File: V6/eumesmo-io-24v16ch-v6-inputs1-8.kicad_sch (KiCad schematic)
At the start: 10 parts, among them U12 OR-3H7-4

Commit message: Renamed all files to eumesmo branding
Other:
- title: ESP 24V 16xIn/16xOut/1-Wire Module -> eumesmo 24V 16xIn/16xOut/1-Wire Module
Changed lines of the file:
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@@
 	(paper "A4")
 	(title_block
-		(title "ESP 24V 16xIn/16xOut/1-Wire Module")
-		(date "2026-02-10")
-		(rev "V6.1")
+		(title "eumesmo 24V 16xIn/16xOut/1-Wire Module")
+		(date "2026-06-13")
+		(rev "V6.2")
 	)
 	(text "I_{LED} = (24V - V_{LED}) / 10k\nI_{LED} = (24V - 2.7V) / 10k\nI_{LED} = 2,13 mA"
@@
 		)
 		(instances
-			(project "esp-24v-16ch-v6"
+			(project "eumesmo-io-24v16ch-v6"
 				(path "/2bc5a21a-1d79-419d-a592-6852cc07b00a/13488771-d756-4bf7-9132-6ca3e4a9325a"
 					(reference "U13")
@@
 		)
 		(instances
-			(project "esp-24v-16ch-v6"
+			(project "eumesmo-io-24v16ch-v6"
 				(path "/2bc5a21a-1d79-419d-a592-6852cc07b00a/13488771-d756-4bf7-9132-6ca3e4a9325a"
 					(reference "D31")
@@
 		)
 		(instances
-			(project "esp-24v-16ch-v6"
+			(project "eumesmo-io-24v16ch-v6"
 				(path "/2bc5a21a-1d79-419d-a592-6852cc07b00a/13488771-d756-4bf7-9132-6ca3e4a9325a"
 					(reference "#PWR0156")
@@
 		)
 		(instances
-			(project "esp-24v-16ch-v6"
+			(project "eumesmo-io-24v16ch-v6"
 				(path "/2bc5a21a-1d79-419d-a592-6852cc07b00a/13488771-d756-4bf7-9132-6ca3e4a9325a"
 					(reference "#PWR0157")
@@
 		)
 		(instances
-			(project "esp-24v-16ch-v6"
+			(project "eumesmo-io-24v16ch-v6"
 				(path "/2bc5a21a-1d79-419d-a592-6852cc07b00a/13488771-d756-4bf7-9132-6ca3e4a9325a"
 					(reference "D32")
@@
 		)
 		(instances
-			(project "esp-24v-16ch-v6"
+			(project "eumesmo-io-24v16ch-v6"
 				(path "/2bc5a21a-1d79-419d-a592-6852cc07b00a/13488771-d756-4bf7-9132-6ca3e4a9325a"
 					(reference "#PWR0153")
@@
 		)
 		(instances
-			(project "esp-24v-16ch-v6"
+			(project "eumesmo-io-24v16ch-v6"
 				(path "/2bc5a21a-1d79-419d-a592-6852cc07b00a/13488771-d756-4bf7-9132-6ca3e4a9325a"
 					(reference "#PWR0154")
@@
 		)
 		(instances
-			(project "esp-24v-16ch-v6"
+			(project "eumesmo-io-24v16ch-v6"
 				(path "/2bc5a21a-1d79-419d-a592-6852cc07b00a/13488771-d756-4bf7-9132-6ca3e4a9325a"
 					(reference "#PWR0152")
@@
 		)
 		(instances
-			(project "esp-24v-16ch-v6"
+			(project "eumesmo-io-24v16ch-v6"
 				(path "/2bc5a21a-1d79-419d-a592-6852cc07b00a/13488771-d756-4bf7-9132-6ca3e4a9325a"
 					(reference "R62")
@@
 		)
 		(instances
-			(project "esp-24v-16ch-v6"
+			(project "eumesmo-io-24v16ch-v6"
 				(path "/2bc5a21a-1d79-419d-a592-6852cc07b00a/13488771-d756-4bf7-9132-6ca3e4a9325a"
 					(reference "#PWR0155")
@@
 		)
 		(instances
-			(project "esp-24v-16ch-v6"
+			(project "eumesmo-io-24v16ch-v6"
 				(path "/2bc5a21a-1d79-419d-a592-6852cc07b00a/13488771-d756-4bf7-9132-6ca3e4a9325a"
 					(reference "C51")
@@
 		)
 		(instances
-			(project "esp-24v-16ch-v6"
+			(project "eumesmo-io-24v16ch-v6"
 				(path "/2bc5a21a-1d79-419d-a592-6852cc07b00a/13488771-d756-4bf7-9132-6ca3e4a9325a"
 					(reference "#PWR0158")
@@
 		)
 		(instances
-			(project "esp-24v-16ch-v6"
+			(project "eumesmo-io-24v16ch-v6"
 				(path "/2bc5a21a-1d79-419d-a592-6852cc07b00a/13488771-d756-4bf7-9132-6ca3e4a9325a"
 					(reference "FB8")
@@
 		)
 		(instances
-			(project "esp-24v-16ch-v6"
+			(project "eumesmo-io-24v16ch-v6"
 				(path "/2bc5a21a-1d79-419d-a592-6852cc07b00a/13488771-d756-4bf7-9132-6ca3e4a9325a"
 					(reference "D33")
@@
 		)
 		(instances
-			(project "esp-24v-16ch-v6"
+			(project "eumesmo-io-24v16ch-v6"
 				(path "/2bc5a21a-1d79-419d-a592-6852cc07b00a/13488771-d756-4bf7-9132-6ca3e4a9325a"
 					(reference "C52")
@@
 		)
 		(instances
-			(project "esp-24v-16ch-v6"
+			(project "eumesmo-io-24v16ch-v6"
 				(path "/2bc5a21a-1d79-419d-a592-6852cc07b00a/13488771-d756-4bf7-9132-6ca3e4a9325a"
 					(reference "R64")
@@
 		)
 		(instances
-			(project "esp-24v-16ch-v6"
+			(project "eumesmo-io-24v16ch-v6"
 				(path "/2bc5a21a-1d79-419d-a592-6852cc07b00a/13488771-d756-4bf7-9132-6ca3e4a9325a"
 					(reference "R63")

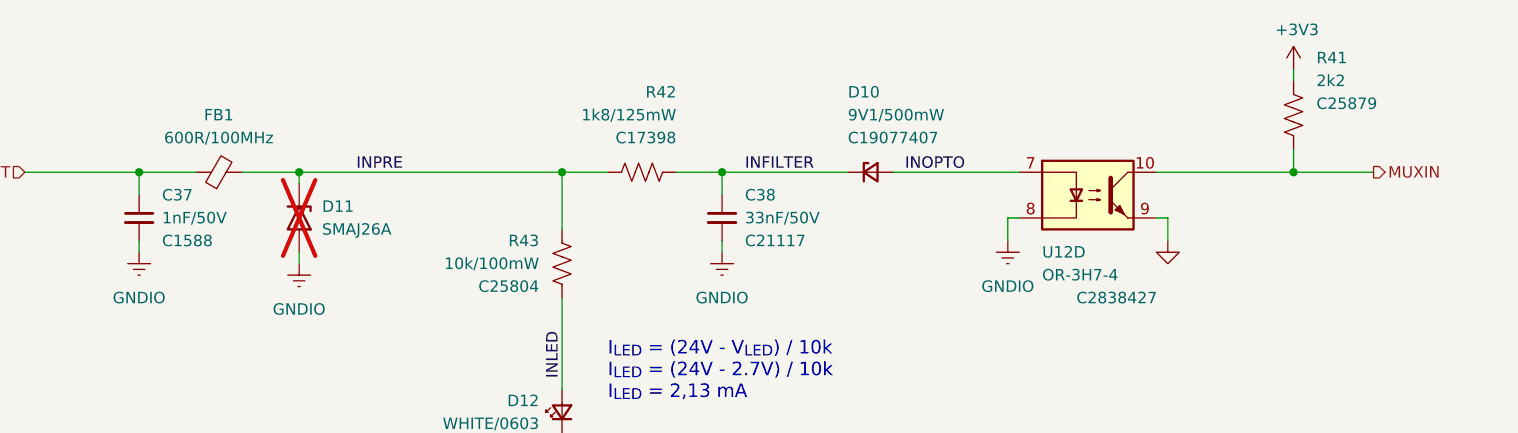
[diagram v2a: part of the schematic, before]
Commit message: Added CPU health LED
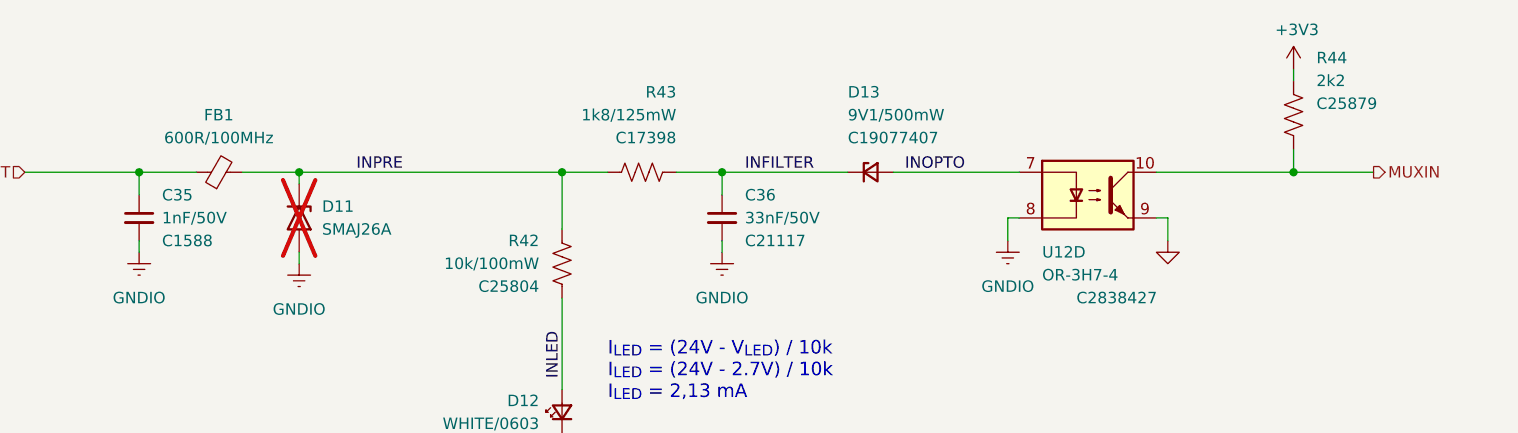
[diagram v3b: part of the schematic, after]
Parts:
- renumbered C37 to C35, C38 to C36, D10 to D13, R43 to R42, R42 to R43, R41 to R44
